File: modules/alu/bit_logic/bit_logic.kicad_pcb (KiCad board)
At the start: 2 copper layers, 67.2 x 34.3 mm, 120 parts, among them J1 PCIe_4x_edge, Q1 2N3904, Q10 2N3906, Q11 2N3906, Q12 2N3906, Q13 2N3906, Q14 2N3906, Q15 2N3906, Q16 2N3904, Q17 2N3904, Q18 2N3904, Q19 2N3904, Q2 2N3904, Q20 2N3904, Q21 2N3904, Q22 2N3904, Q23 2N3904, Q24 2N3904, Q25 2N3906, Q26 2N3906, Q27 2N3906, Q28 2N3906, Q29 2N3904, Q3 2N3904, Q30 2N3906, Q31 2N3906, Q32 2N3904, Q33 2N3906, Q34 2N3906, Q35 2N3904, Q36 2N3904, Q37 2N3906, Q38 2N3904, Q39 2N3904, Q4 2N3904, Q40 2N3904, Q41 2N3906, Q42 2N3906, Q43 2N3904, Q44 2N3904, Q45 2N3906, Q46 2N3906, Q47 2N3906, Q48 2N3904, Q49 2N3904, Q5 2N3904, Q50 2N3904, Q51 2N3906, Q52 2N3906, Q53 2N3904, Q54 2N3904, Q55 2N3904, Q56 2N3904, Q57 2N3906, Q6 2N3904, Q7 2N3904, Q8 2N3904, Q9 2N3904

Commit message: Some more work on power routing.
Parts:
- moved R42 4.88 mm to (157.4, 77.4), turned to -90 degrees
- moved Q47 4.66 mm to (163.3, 89.1), turned to 180 degrees
- moved D11 3.79 mm to (163.8, 93.2), turned to -90 degrees
- moved R43 3.31 mm to (153.3, 77.1), turned to 0 degrees
- moved R38 1.24 mm to (166.4, 90.9)
- moved Q41 1.21 mm to (163.4, 100.1), turned to 180 degrees
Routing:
- net VCC: track 122.6 -> 197.9 mm, vias 0 -> 4
- net /OUT_A: track 180.8 -> 158.5 mm, vias 4 -> 6
- net /OUT_S: track 43.8 -> 35.1 mm
- net /IN_INV_B: track 85.6 -> 92.4 mm
- net /XX: track 35.3 -> 41.1 mm
- net Net-(D4-K): track 48.8 -> 52.3 mm
- net /OUT_G: track 207.1 -> 210.1 mm
- net Net-(Q16-E): track 13.8 -> 15.6 mm
- net Net-(Q51-E): track 12.4 -> 10.8 mm
- net Net-(D11-K): track 9.40 -> 10.6 mm
- net Net-(D6-K): track 129.9 -> 131.1 mm
- net /OUT_P: track 129.3 -> 128.5 mm
- net Net-(D8-K): track 19.7 -> 20.5 mm
- net Net-(D8-A): track 4.83 -> 5.46 mm

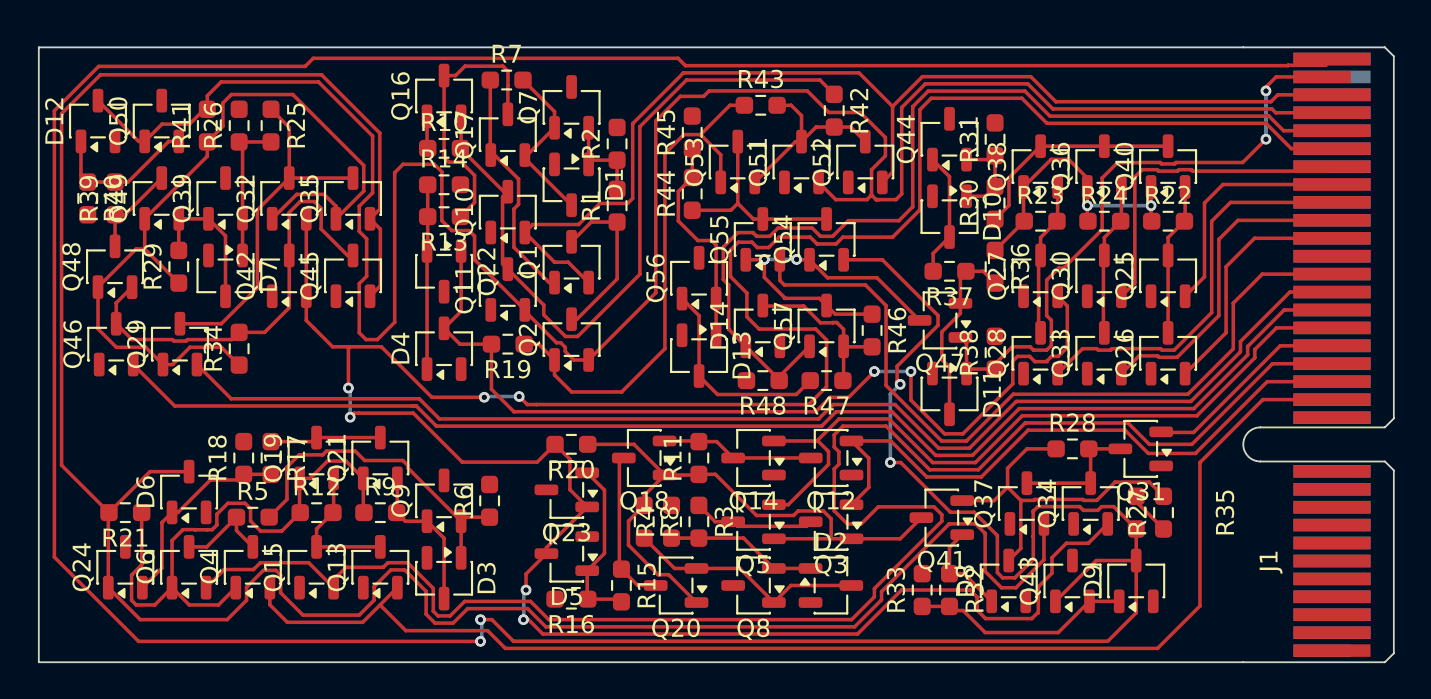
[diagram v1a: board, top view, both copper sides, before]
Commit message: PCB is more or less done. It's DRC clean but needs bypass caps and some power optimizations.
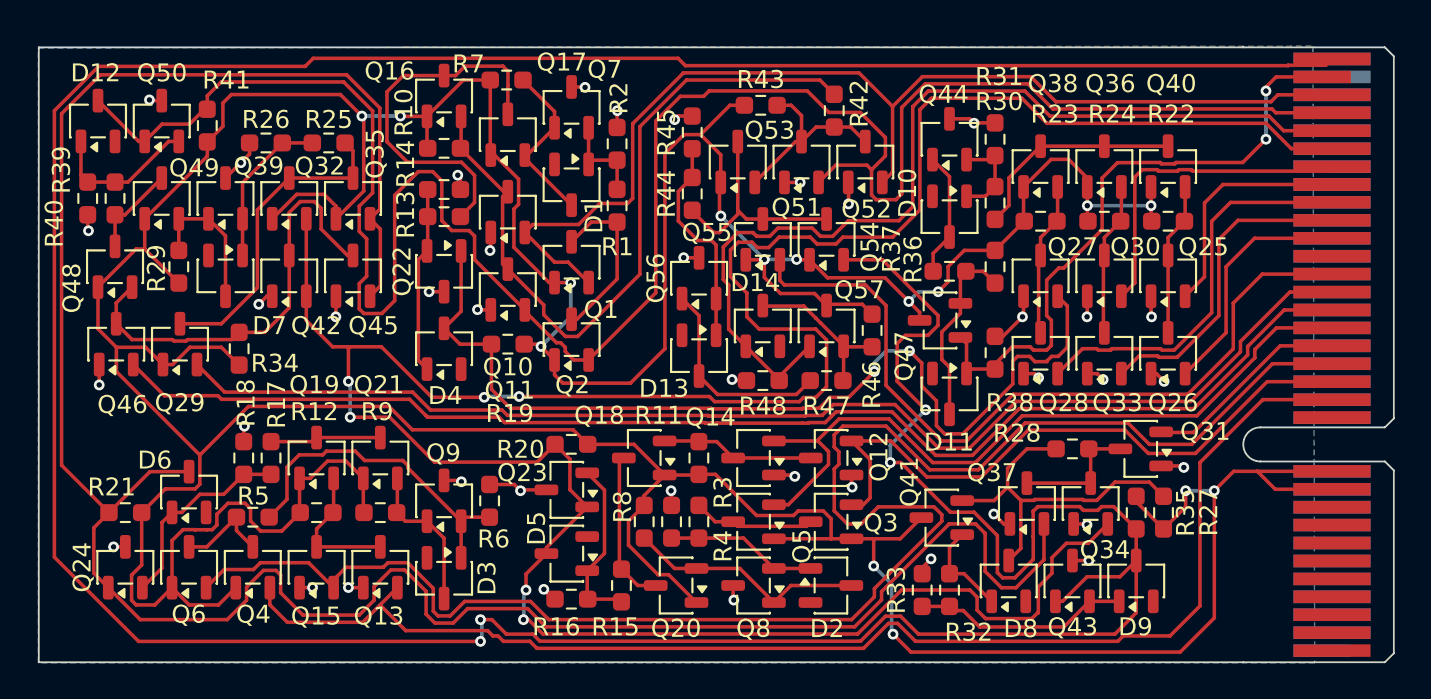
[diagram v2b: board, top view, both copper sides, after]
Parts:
- moved R25 3.36 mm to (129.2, 79.2), turned to 180 degrees
- moved R26 1.78 mm to (125.7, 79.2), turned to 180 degrees
- moved R14 0.27 mm to (135.6, 81.8)
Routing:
- net VCC: track 197.9 -> 309.2 mm, vias 4 -> 15
- net GND: track 0.00 -> 45.3 mm, vias 0 -> 40
- net Net-(Q16-E): track 15.6 -> 20.9 mm
- net /OUT_P: track 128.5 -> 125.1 mm
- net /OUT_G: track 210.1 -> 212.8 mm
- net Net-(Q29-E): track 19.8 -> 17.7 mm
- net Net-(D4-K): track 52.3 -> 54.0 mm
- net Net-(D6-K): track 131.1 -> 132.6 mm
- net Net-(Q53-E): track 11.5 -> 12.7 mm
- net /IN_B: track 73.8 -> 74.6 mm
- net Net-(D7-A): track 8.19 -> 8.87 mm
- net Net-(D14-K): track 9.55 -> 8.99 mm
- added copper zone on B.Cu, net GND
